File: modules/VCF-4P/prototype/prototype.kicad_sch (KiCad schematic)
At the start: 38 parts, among them J1 Conn_01x09, U1 TL074, U2 SSI2140

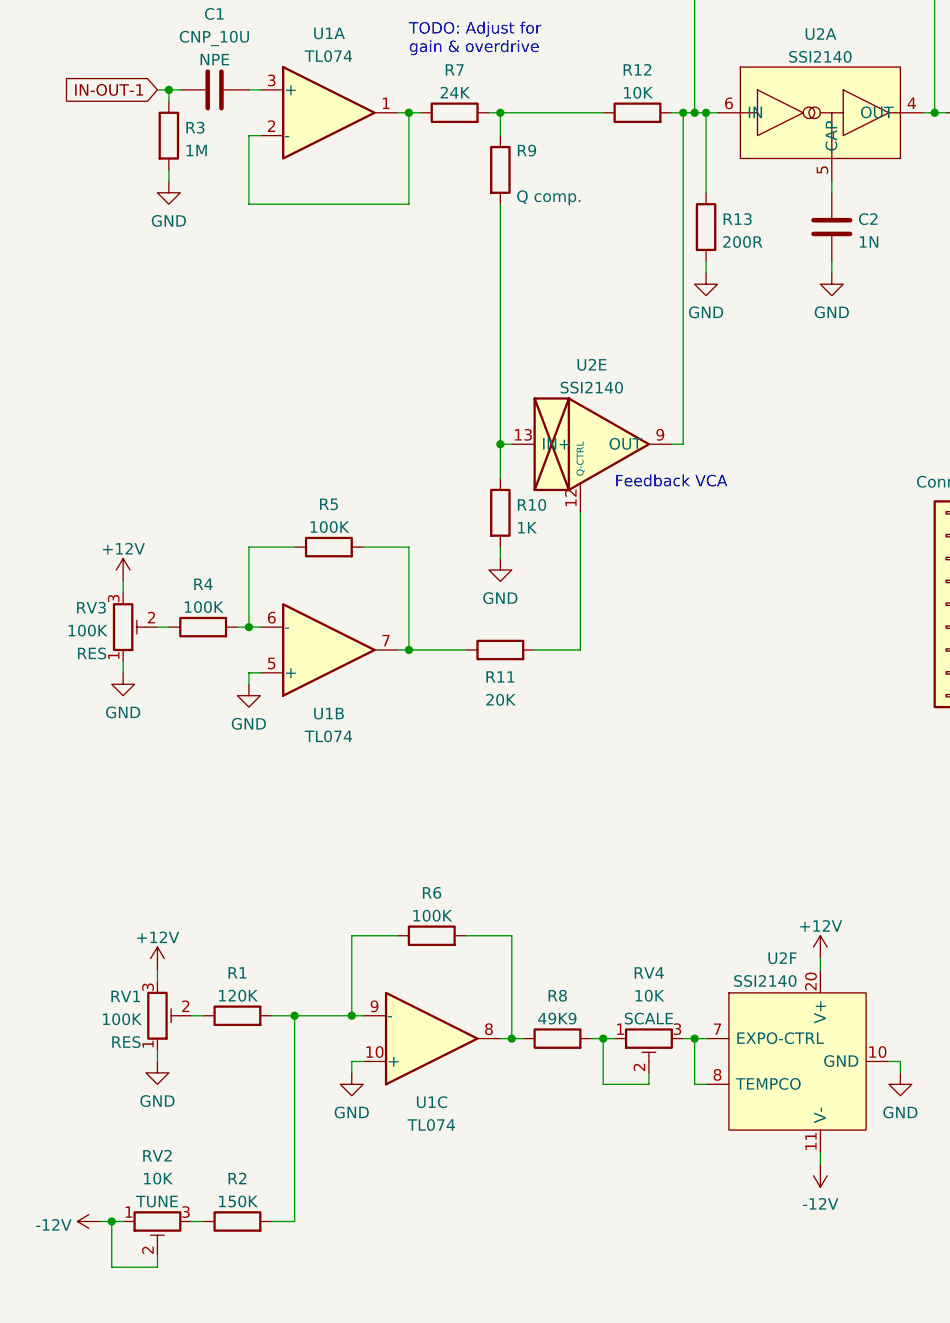
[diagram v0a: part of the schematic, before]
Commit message: VCF-4P: Breadboard prototype - wip
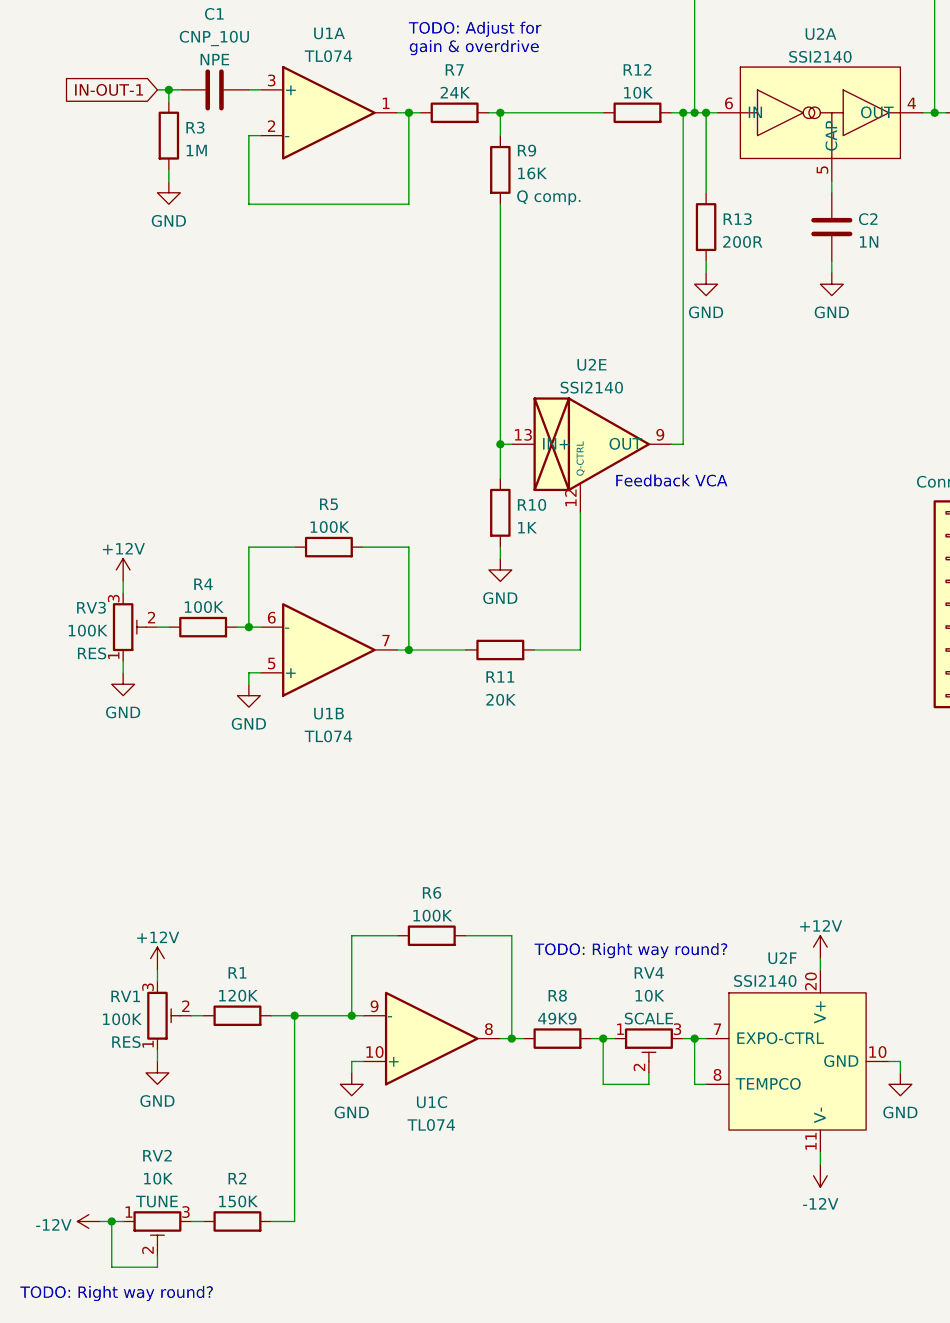
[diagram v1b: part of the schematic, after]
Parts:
- R9: value (none) -> 16K; footprint (none) -> -lmp-misc:R_Axial_DIN0207_L6.3mm_D2.5mm_P7.62mm_Horizontal
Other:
- note added: "TODO: Right way round?"
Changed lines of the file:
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@@
+    (effects (font (size 1.27 1.27)) (justify left bottom))
+  )
+  (text "TODO: Right way round?" (at 24.13 173.99 0)
+    (effects (font (size 1.27 1.27)) (justify left bottom))
+  )
+  (text "TODO: Right way round?" (at 81.28 135.89 0)
     (effects (font (size 1.27 1.27)) (justify left bottom))
   )
@@
       (effects (font (size 1.27 1.27)) (justify left))
     )
-    (property "Value" "" (id 1) (at 79.248 48.6938 0)
-      (effects (font (size 1.27 1.27)) (justify left))
-    )
-    (property "Footprint" "" (id 2) (at 75.692 48.26 90)
-      (effects (font (size 1.27 1.27)) hide)
-    )
+    (property "Value" "16K" (id 1) (at 79.248 48.6938 0)
+      (effects (font (size 1.27 1.27)) (justify left))
+    )
+    (property "Footprint" "-lmp-misc:R_Axial_DIN0207_L6.3mm_D2.5mm_P7.62mm_Horizontal" (id 2) (at 75.692 48.26 90)
+      (effects (font (size 1.27 1.27)) hide)
+    )

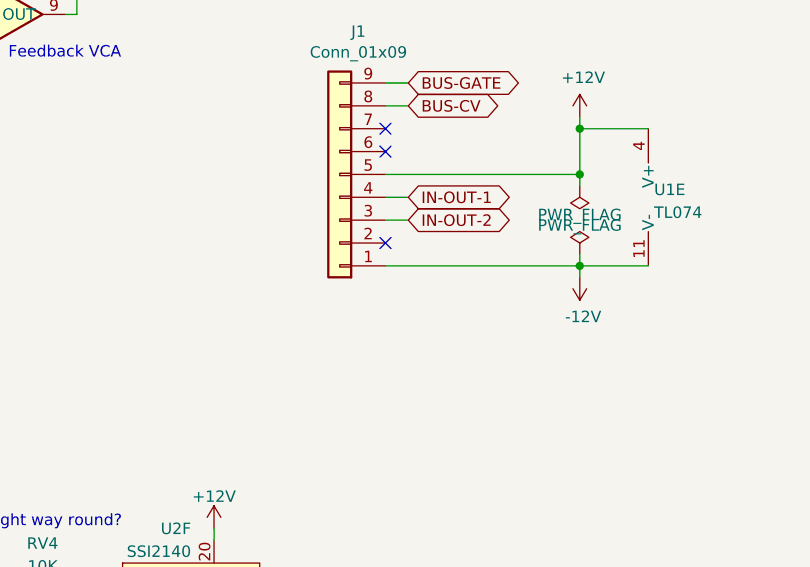
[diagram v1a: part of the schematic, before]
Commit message: VCF-4P: Breadboard prototype - done
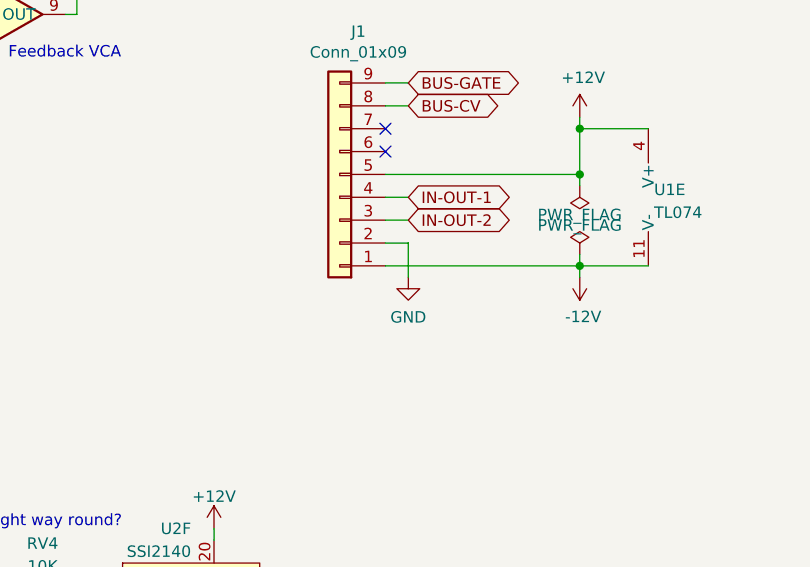
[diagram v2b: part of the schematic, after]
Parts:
- R10, R11, R13, R15, R16, R19, R22, R23, R24, R3, R5, R6: footprint -lmp-misc:R_Axial_DIN0207_L6.3mm_D2.5mm_P7.62mm_Horizontal -> -lmp-stripboard:SB_Gen_1
- R14, R17, R20, R26: footprint -lmp-misc:R_Axial_DIN0207_L6.3mm_D2.5mm_P7.62mm_Horizontal -> -lmp-stripboard:SB_Gen_2
- R25: footprint -lmp-misc:R_Axial_DIN0207_L6.3mm_D2.5mm_P10.16mm_Horizontal -> -lmp-stripboard:SB_Gen_2
- R4: footprint -lmp-misc:R_Axial_DIN0207_L6.3mm_D2.5mm_P7.62mm_Horizontal -> -lmp-stripboard:SB_Gen_4
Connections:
- net GND: now also J1.2 (Pin_2)
- no-connect marks 3 -> 2

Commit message: VCF-4P: update prototype
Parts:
- RV1: value 100K -> (none); footprint -lmp-misc:Potentiometer_Bourns_3310R_Top -> (none); Label RES -> CUTOFF
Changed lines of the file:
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@@
       (effects (font (size 1.27 1.27)) (justify right))
     )
-    (property "Value" "100K" (id 1) (at 37.5921 142.6738 0)
+    (property "Value" "" (id 1) (at 37.5921 142.6738 0)
       (effects (font (size 1.27 1.27)) (justify right))
     )
-    (property "Footprint" "-lmp-misc:Potentiometer_Bourns_3310R_Top" (id 2) (at 39.37 142.24 0)
+    (property "Footprint" "" (id 2) (at 39.37 142.24 0)
       (effects (font (size 1.27 1.27)) hide)
     )
@@
       (effects (font (size 1.27 1.27)) hide)
     )
-    (property "Label" "RES" (id 4) (at 37.5921 145.2107 0)
+    (property "Label" "CUTOFF" (id 4) (at 37.5921 145.2107 0)
       (effects (font (size 1.27 1.27)) (justify right))
     )
@@
   (symbol (lib_id "-lmp-power:GND") (at 134.62 107.95 0) (unit 1)
     (in_bom yes) (on_board yes) (fields_autoplaced)
-    (property "Reference" "#PWR?" (id 0) (at 134.62 114.3 0)
+    (property "Reference" "#PWR0101" (id 0) (at 134.62 114.3 0)
       (effects (font (size 1.27 1.27)) hide)
     )
@@
     )
     (path "/525f23b9-a23c-4305-afe1-22811746f220"
-      (reference "#PWR?") (unit 1) (value "GND") (footprint "")
+      (reference "#PWR0101") (unit 1) (value "GND") (footprint "")
     )
     (path "/62009989-8103-49af-b226-a7bac174e878"

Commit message: VCF-4P: prototype - wip
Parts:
- C1: value CNP_10U -> 10U
- R13, R16, R19, R24: Value2 1%, 1/6 W -> 220R
- R2: value 150K -> 153K; Value2 1%, 1/6 W -> 150K
- R7, R9: Value2 1%, 1/6 W -> 15K
- R8: value 49K9 -> 53K; Value2 1%, 1/6 W -> 49K9
- RV1: value (none) -> 100K; footprint (none) -> -lmp-misc:Potentiometer_Bourns_3310R_Top
- RV2, RV4: value 10K -> 5K; Value2 (none) -> 10K
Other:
- note added: "TODO: Good adjustment range?"

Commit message: VCF-4P - wip
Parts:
- removed R5: 100K, -lmp-stripboard:SB_Gen_1, symbol -lmp:R_1%_0W166
- R21: value 120K -> 30K
- R23: value 30K -> 120K
- R4: footprint -lmp-stripboard:SB_Gen_4 -> -lmp-stripboard:SB_Gen_2
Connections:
- net +12V: now also R4.2; no longer RV3.3
- net GND: no longer U1.5 (+)
- net at R4.1: now also RV3.3; no longer RV3.2
- net at U1.6 (-): now also R11.1, U1.7; no longer R4.2
- new net: RV3.2, U1.5 (+)
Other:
- moved on the sheet: R4, RV3

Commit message: VCF-4P: prototype - tweak cutoff CV
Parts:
- R1: value 120K -> 100K
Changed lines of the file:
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@@
     (in_bom yes) (on_board yes) (fields_autoplaced)
     (property "Reference" "R1" (id 0) (at 48.26 137.5242 90))
-    (property "Value" "120K" (id 1) (at 48.26 140.0611 90))
+    (property "Value" "100K" (id 1) (at 48.26 140.0611 90))
     (property "Footprint" "-lmp-misc:R_Axial_DIN0207_L6.3mm_D2.5mm_P7.62mm_Horizontal" (id 2) (at 48.26 144.018 90)
       (effects (font (size 1.27 1.27)) hide)
@@
     )
     (path "/561a72a5-4948-4d8a-a9ef-ff63b0ec757a"
-      (reference "R1") (unit 1) (value "120K") (footprint "-lmp-misc:R_Axial_DIN0207_L6.3mm_D2.5mm_P7.62mm_Horizontal")
+      (reference "R1") (unit 1) (value "100K") (footprint "-lmp-misc:R_Axial_DIN0207_L6.3mm_D2.5mm_P7.62mm_Horizontal")
     )
     (path "/5f9ab64b-38ff-4889-9d59-ea8e53307840"
